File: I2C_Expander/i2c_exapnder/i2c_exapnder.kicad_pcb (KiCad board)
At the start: 2 copper layers, 60.9 x 50 mm, 8 parts, among them J1 Conn_01x10, J2 Conn_01x05, J3 Conn_01x05, J4 Conn_01x05

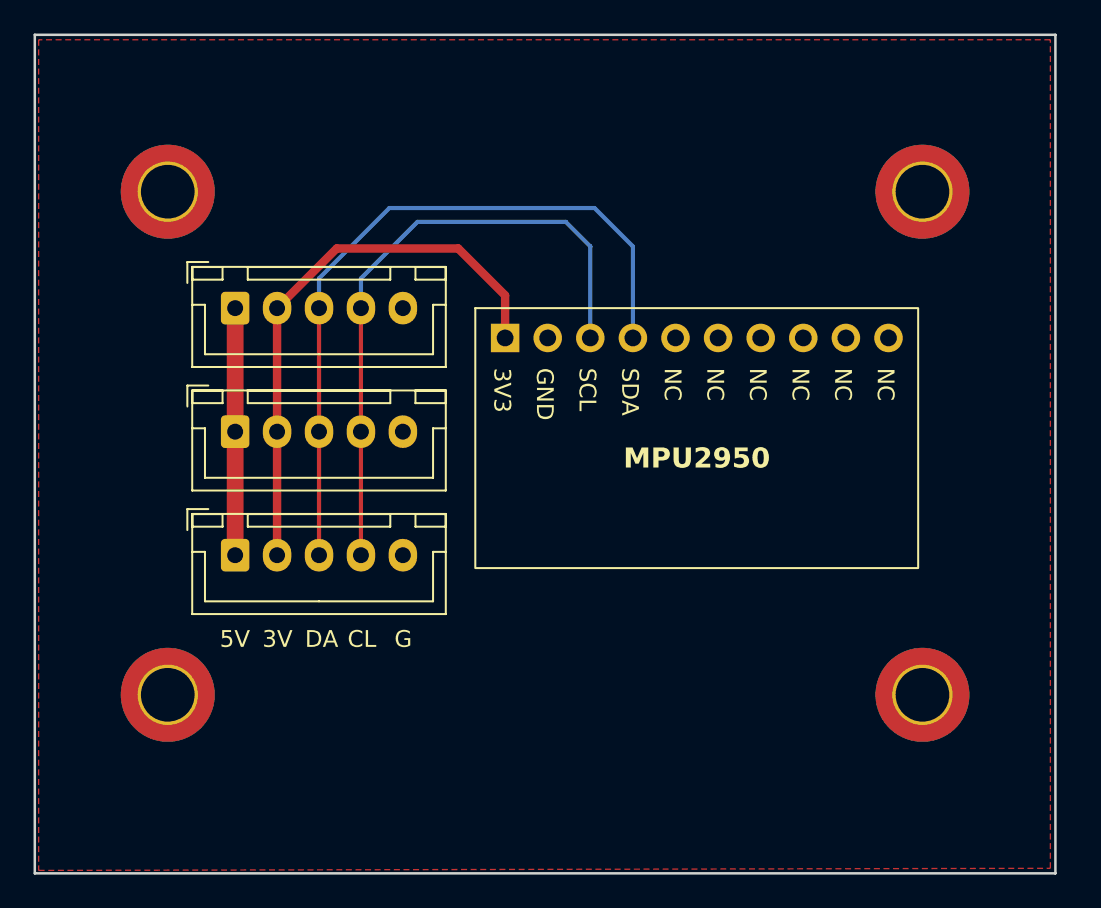
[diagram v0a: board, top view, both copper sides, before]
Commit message: Add logo and text to I2C Expander
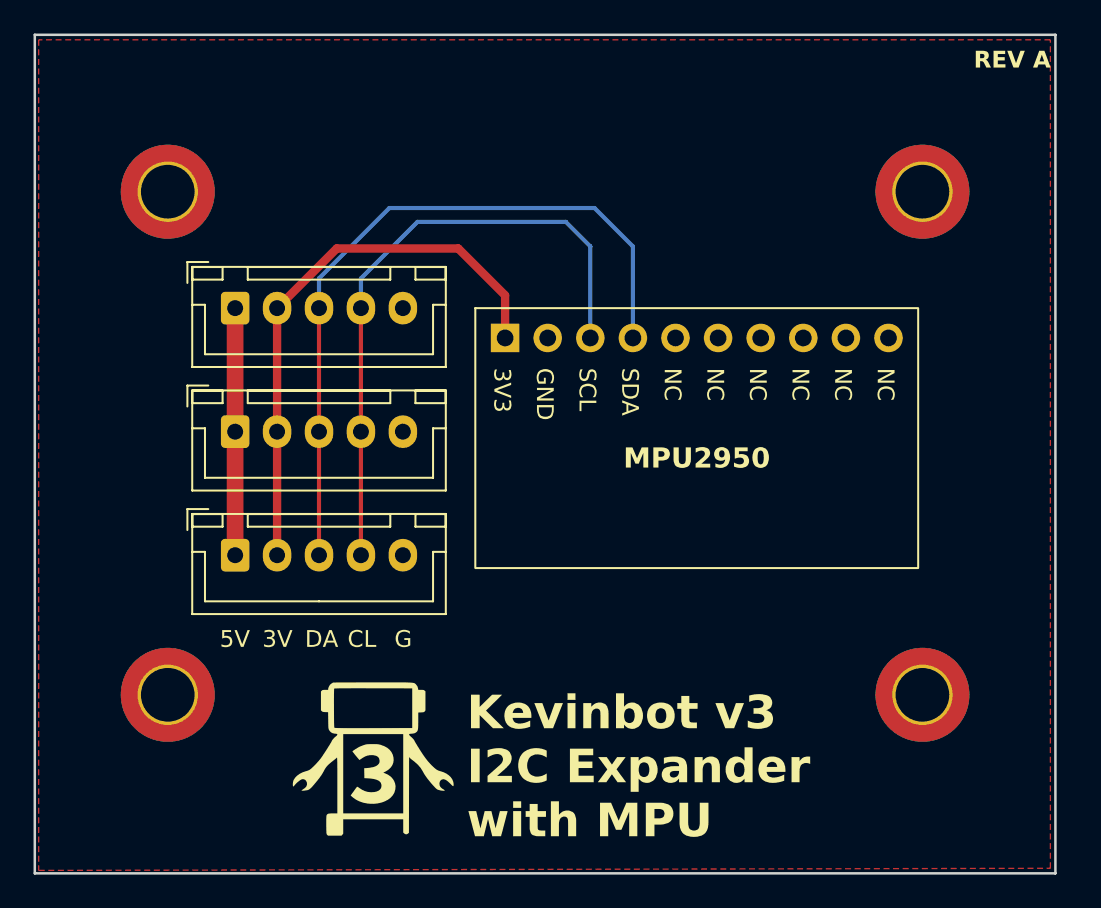
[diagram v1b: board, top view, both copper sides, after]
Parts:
- added G***: LOGO, Logos:KevinbotLogo10mm, F.Cu at (140.5, 116.5)
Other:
- board text added: "Kevinbot v3 I2C Expander with MPU"
- board text added: "REV A"
